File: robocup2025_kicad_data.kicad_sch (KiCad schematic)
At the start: 13 parts, among them M7 Motor_Servo, U1 RASPBERRY_PI_4B_4GB, U2 ESP32-DEVKITC-32E

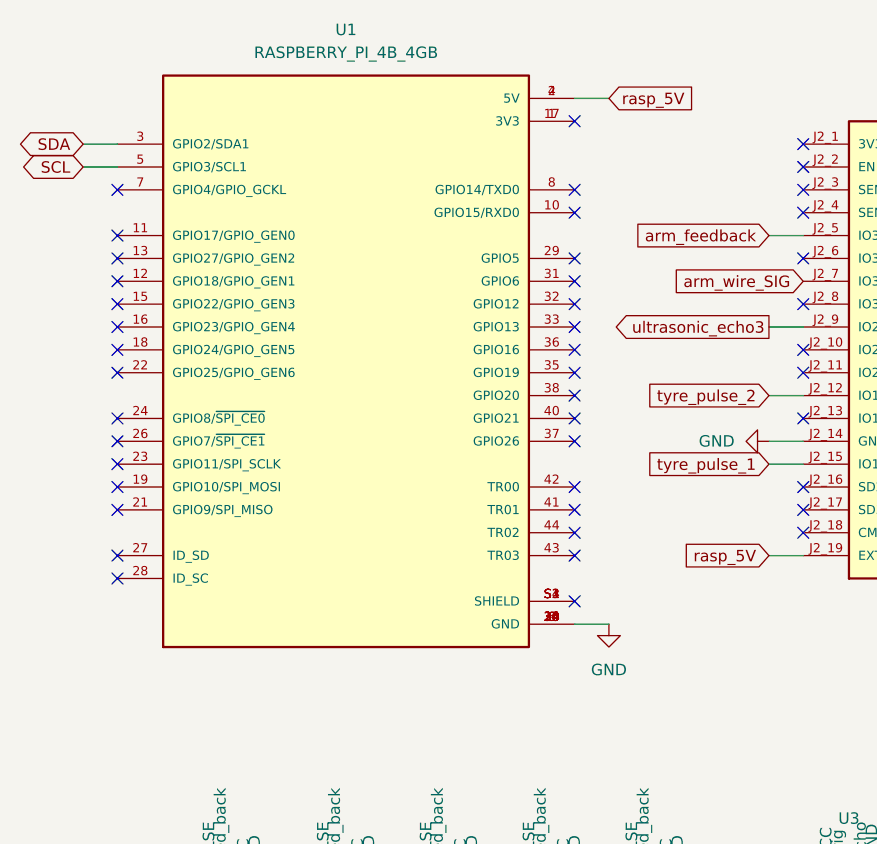
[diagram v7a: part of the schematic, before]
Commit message: rm: Removed raspberrypi object
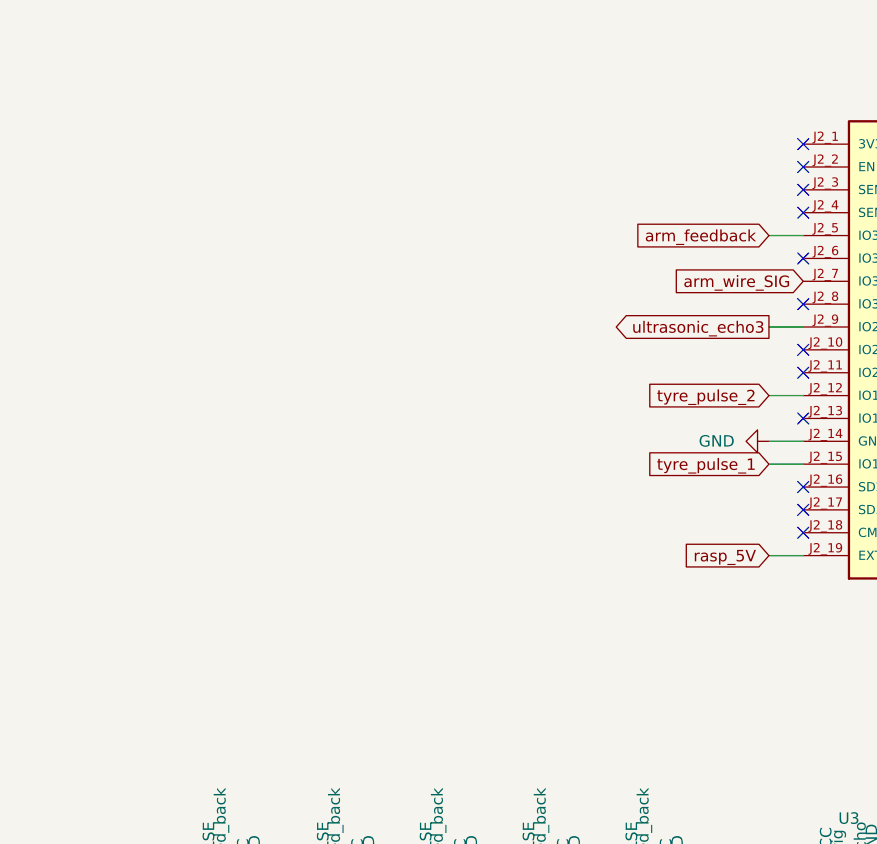
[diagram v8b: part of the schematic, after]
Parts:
- removed U1: RASPBERRY_PI_4B_4GB, robo:raspberrypi5 small, symbol robo:RASPBERRY_PI_4B_4GB
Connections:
- no-connect marks 55 -> 23
